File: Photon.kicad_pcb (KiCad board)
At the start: 2 copper layers, 21.2 x 74.4 mm, 53 parts, among them J1 USB_C_Receptacle_USB2.0_14P, Q1 IRLML6402, Q2 IRLML6402, SW1 TS-1088-AR02016, U1 ATtiny13A-S, U2 RT8059GJ5, U3 TP4056, U4 BCR421UW6-7, U5 DW01A, U6 FS8205A, U7 BCR421UW6-7

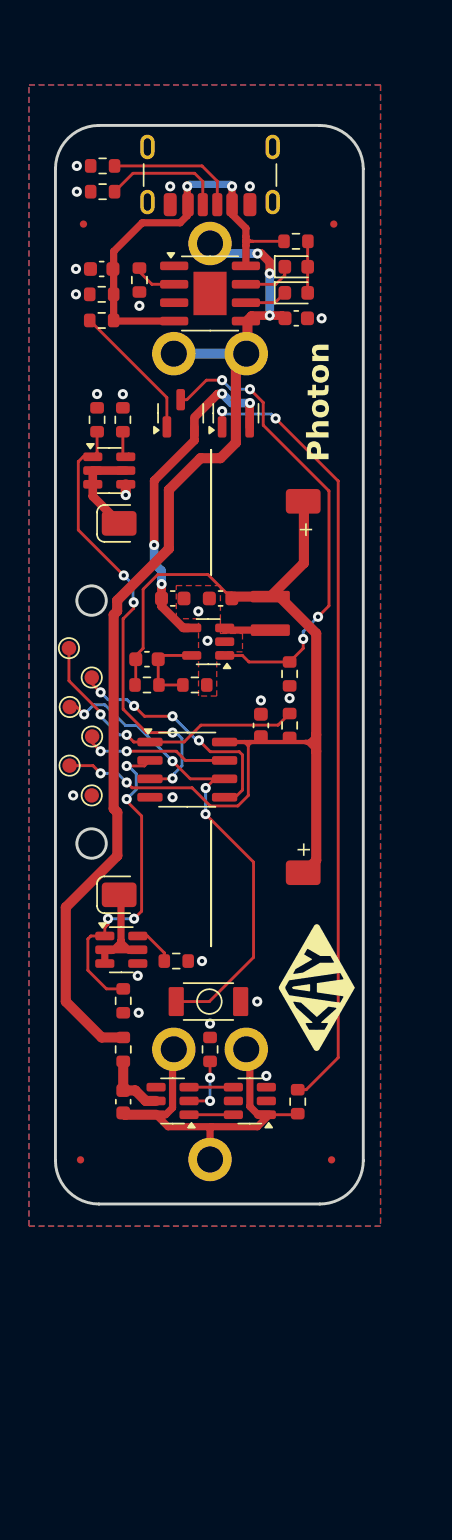
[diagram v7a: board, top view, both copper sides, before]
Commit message: Swapped out MCU
- not completed (WIP)
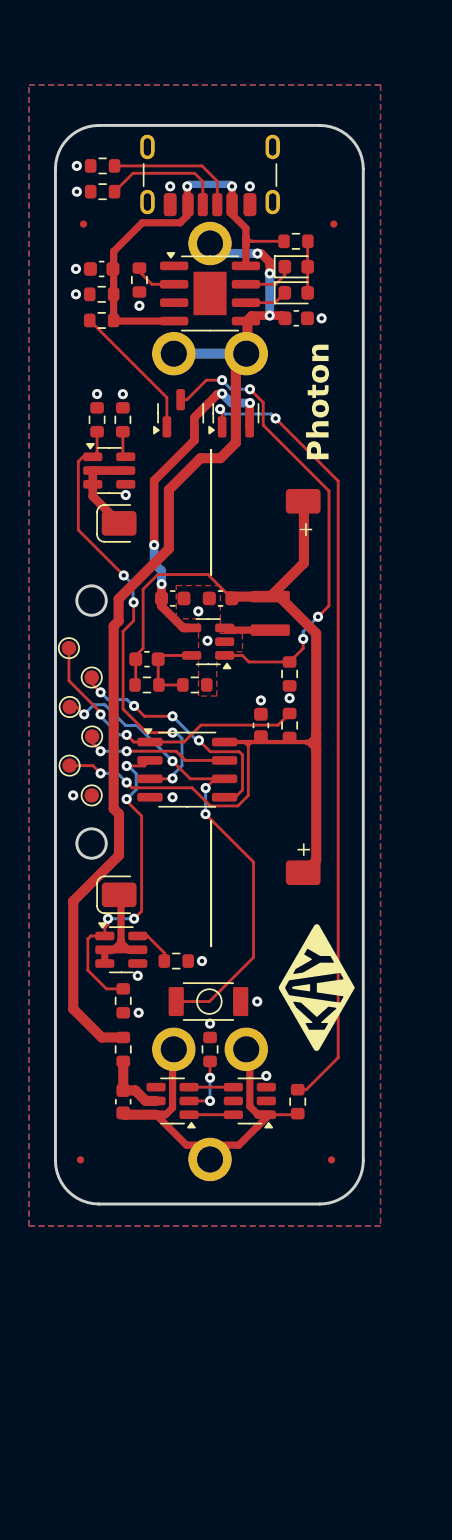
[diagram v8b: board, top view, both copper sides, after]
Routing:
- net /Bat-: track 26.2 -> 25.0 mm
- net GND: track 0.74 -> 0.00 mm
